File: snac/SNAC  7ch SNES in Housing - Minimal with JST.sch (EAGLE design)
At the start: 8 parts, among them U1 PMIC-LDO-XC6206P332MR-G(SOT23), X2 JST-XH-09-PIN-LONG-PAD

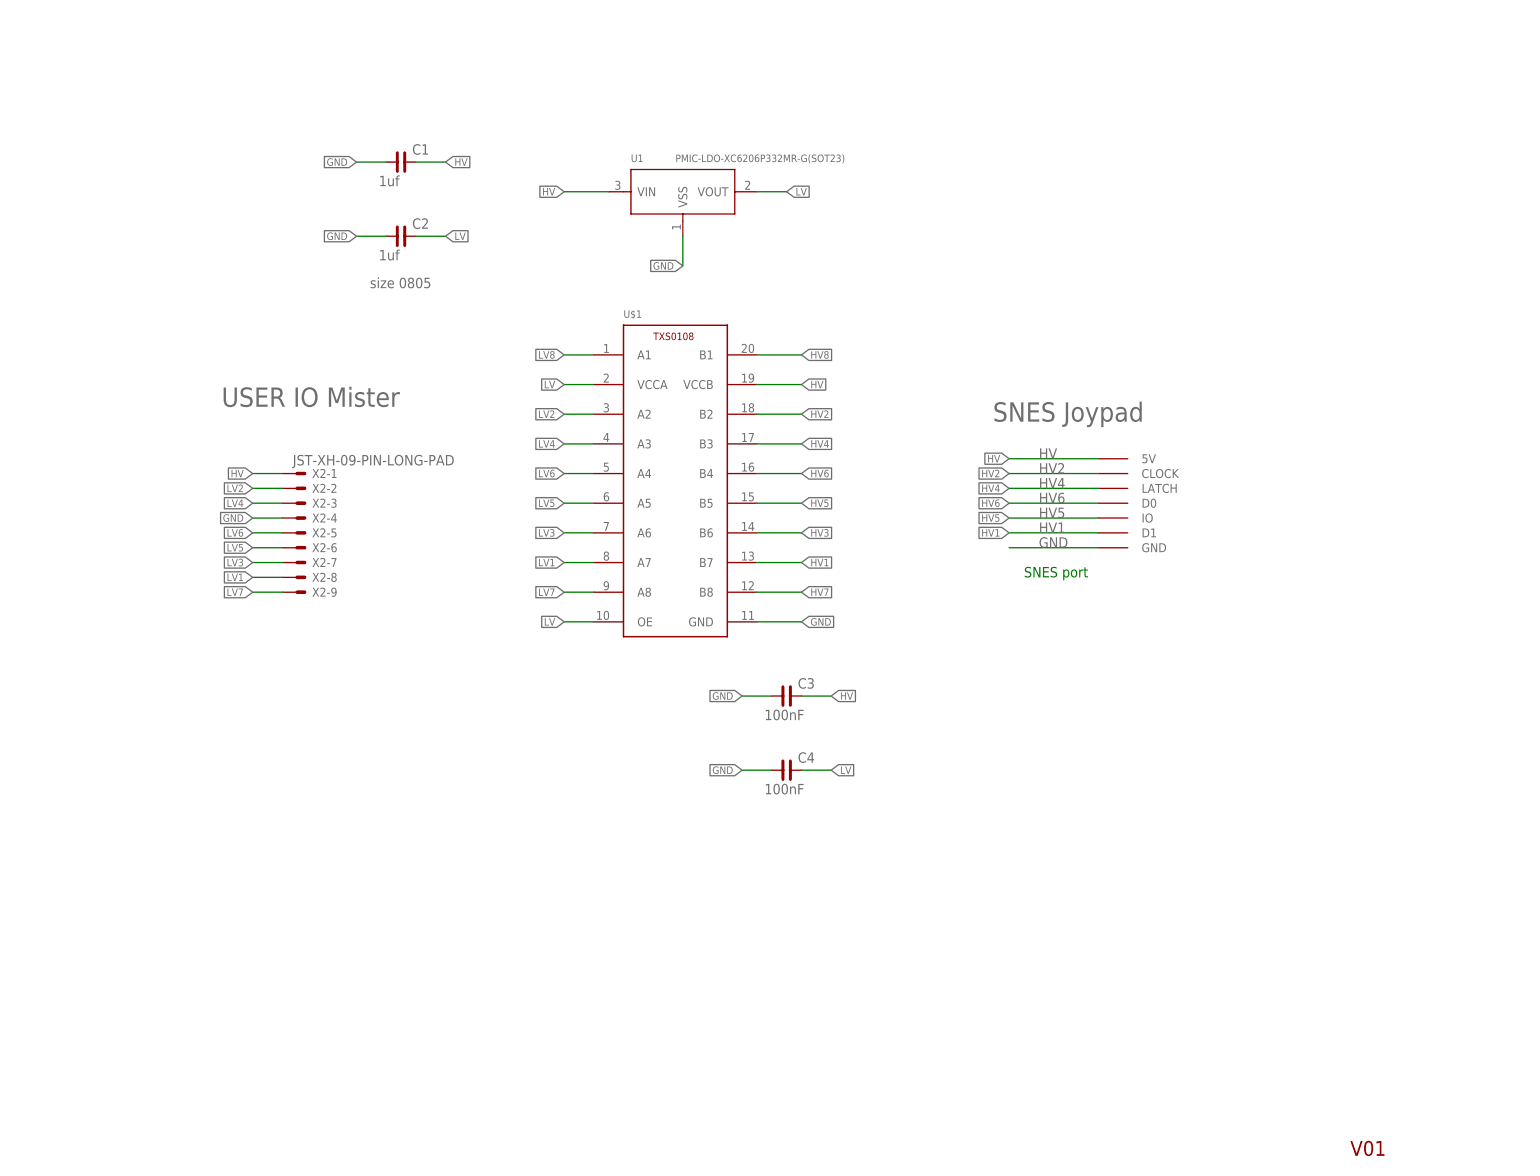
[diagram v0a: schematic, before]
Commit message: added reversed JST footprint to SNES SNAC Minimal
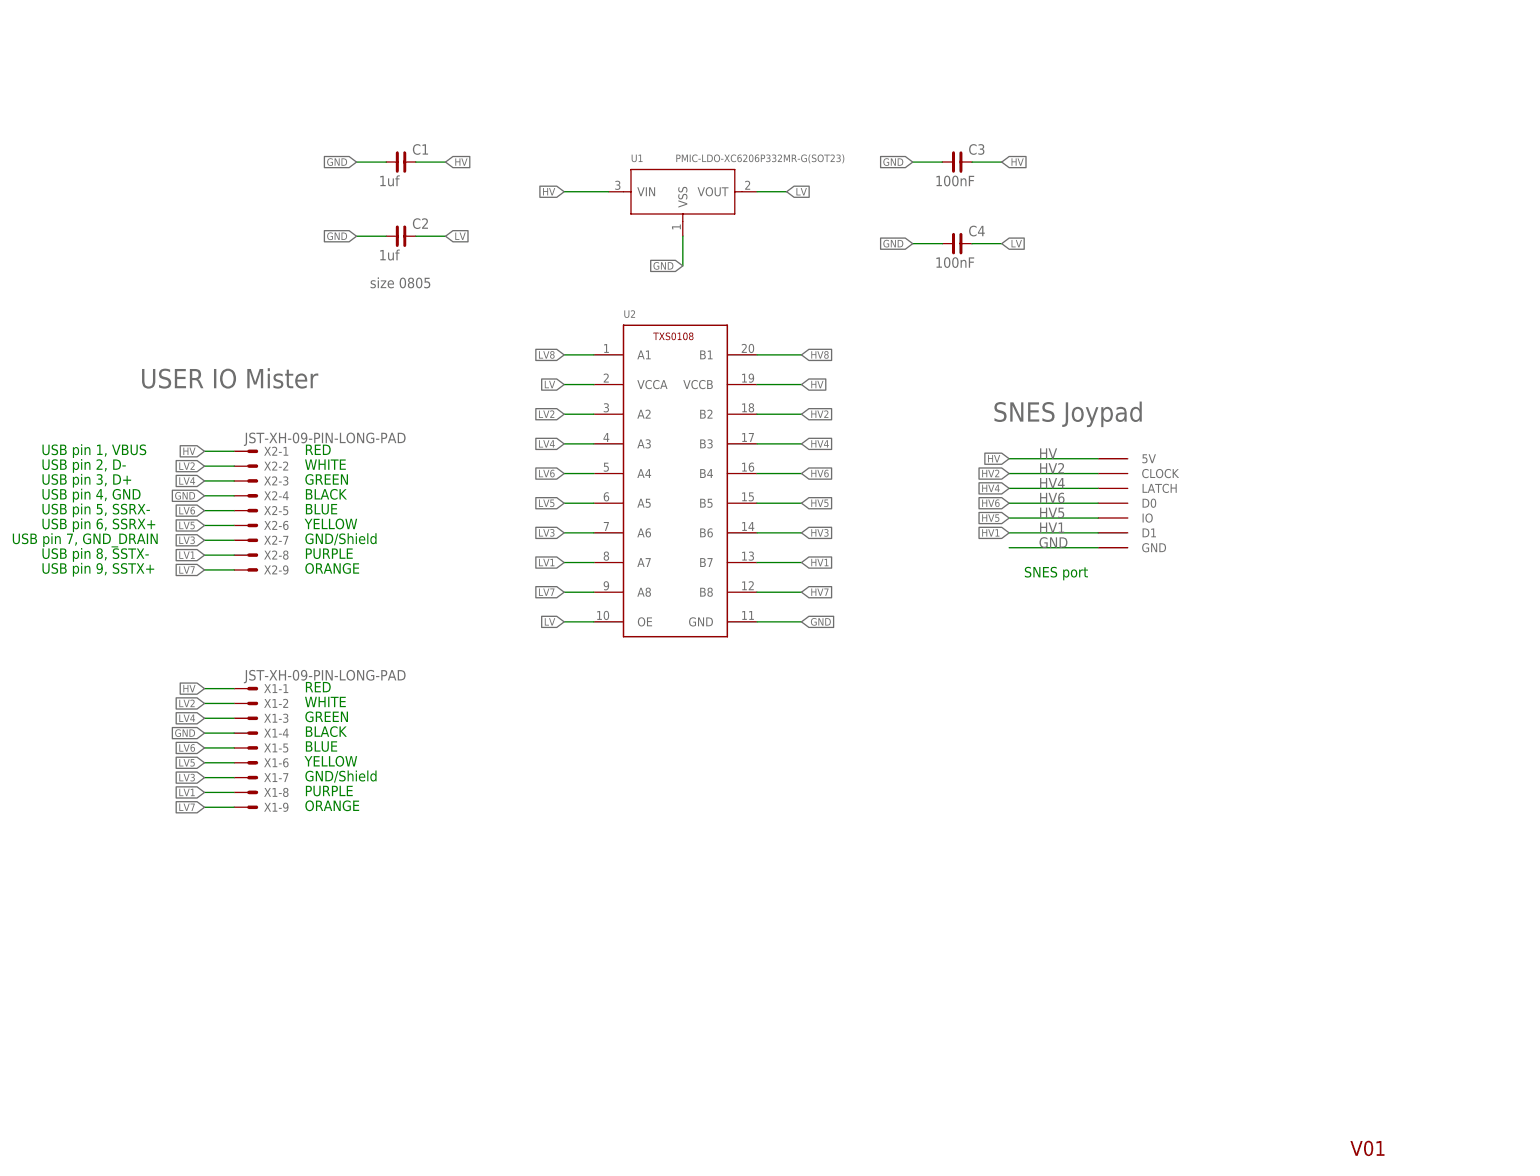
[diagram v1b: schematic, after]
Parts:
- added X1: JST-XH-09-PIN-LONG-PAD, Rembrandt Electronics - JST XH Connectors v1-0:JST-XH-09-PIN-LONG-PAD
- renumbered U$1 to U2, U$3 to SNES_CON
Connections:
- net GND: now also X1-4.S
- net HV: now also X1-1.S
- net LV1: now also X1-8.S
- net LV2: now also X1-2.S
- net LV3: now also X1-7.S
- net LV4: now also X1-3.S
- net LV5: now also X1-6.S
- net LV6: now also X1-5.S
- net LV7: now also X1-9.S
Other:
- note added: "BLACK"
- note added: "BLUE"
- note added: "GND/Shield"
- note added: "GREEN"
- note added: "ORANGE"
- note added: "PURPLE"
- note added: "RED"
- note added: "USB pin 1, VBUS"
- note added: "USB pin 2, D-"
- note added: "USB pin 3, D+"
- note added: "USB pin 4, GND"
- note added: "USB pin 5, SSRX-"
- note added: "USB pin 6, SSRX+"
- note added: "USB pin 7, GND_DRAIN"
- note added: "USB pin 8, SSTX-"
- note added: "USB pin 9, SSTX+"
- note added: "WHITE"
- note added: "YELLOW"
- moved on the sheet: C3, C4, X2-1, X2-2, X2-3, X2-4, X2-5, X2-6, X2-7, X2-8, X2-9

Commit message: removed the Compact, TXS chip, and SMS3D with USB3 plug versions
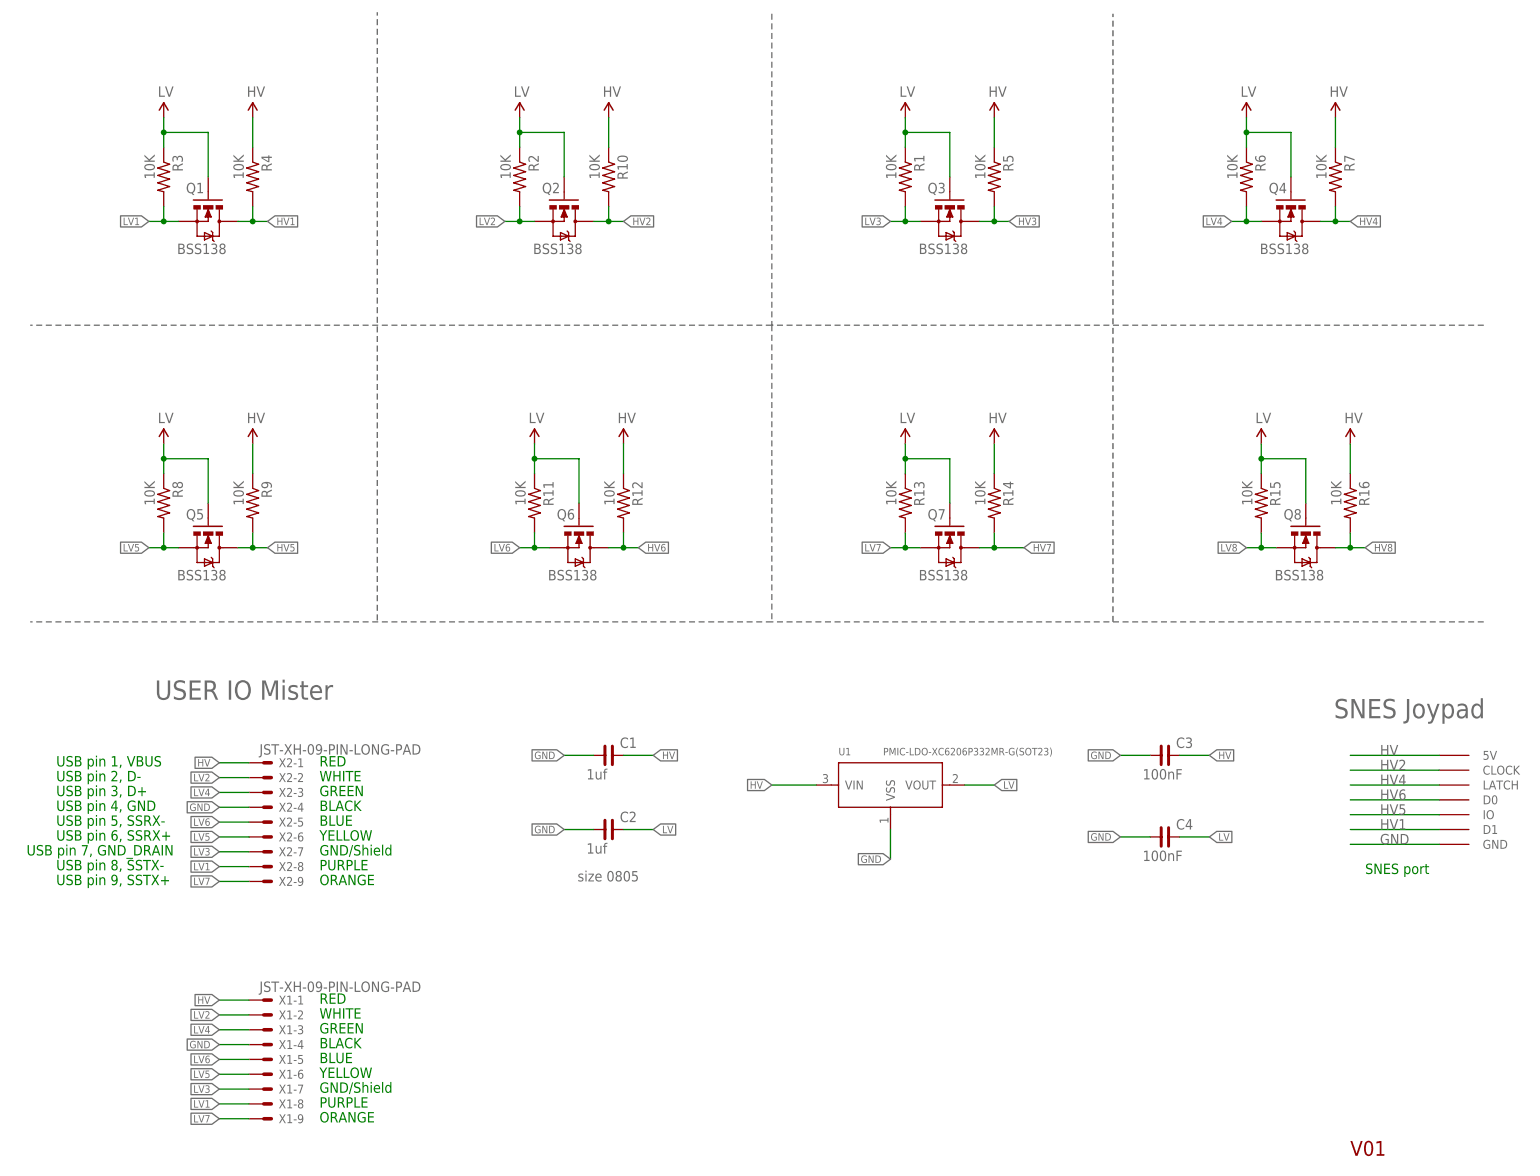
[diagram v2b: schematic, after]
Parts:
- removed U2: TXS0108, FaBo-LevelTranslator:TXS0108
- added Q1, Q2, Q3, Q4, Q5, Q6, Q7, Q8: BSS138, SparkFun:MOSFET-NCHANNELSMD
- added R1, R10, R11, R12, R13, R14, R15, R16, R2, R3, R4, R5, R6, R7, R8, R9: 10K, SparkFun:RESISTOR0603-RES
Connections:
- net GND: no longer U2.GND
- net HV: now also R10.1, R12.1, R14.1, R16.1, R4.1, R5.1, R7.1, R9.1; no longer U2.VCCB
- net HV1: now also Q1.D, R4.2; no longer U2.B7
- net HV2: now also Q2.D, R10.2; no longer U2.B2
- net HV3: now also Q3.D, R5.2; no longer U2.B6
- net HV4: now also Q4.D, R7.2; no longer U2.B3
- net HV5: now also Q5.D, R9.2; no longer U2.B5
- net HV6: now also Q6.D, R12.2; no longer U2.B4
- net HV7: now also Q7.D, R14.2; no longer U2.B8
- net HV8: now also Q8.D, R16.2; no longer U2.B1
- net LV: now also Q1.G, Q2.G, Q3.G, Q4.G, Q5.G, Q6.G, Q7.G, Q8.G, R1.1, R11.1, R13.1, R15.1, R2.1, R3.1, R6.1, R8.1; no longer U2.OE, U2.VCCA
- net LV1: now also Q1.S, R3.2; no longer U2.A7
- net LV2: now also Q2.S, R2.2; no longer U2.A2
- net LV3: now also Q3.S, R1.2; no longer U2.A6
- net LV4: now also Q4.S, R6.2; no longer U2.A3
- net LV5: now also Q5.S, R8.2; no longer U2.A5
- net LV6: now also Q6.S, R11.2; no longer U2.A4
- net LV7: now also Q7.S, R13.2; no longer U2.A8
- net LV8: now also Q8.S, R15.2; no longer U2.A1
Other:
- moved on the sheet: C1, C2, C3, C4, U1, X1-1, X1-2, X1-3, X1-4, X1-5, X1-6, X1-7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

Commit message: removed one cap from the SNES SNAC JST, as it was overkill
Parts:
- removed C4: 100nF, rc-master-smd:C_0805
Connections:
- net GND: no longer C4.1
- net HV: no longer C3.2
- net LV: now also C3.2; no longer C4.2
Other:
- moved on the sheet: C3
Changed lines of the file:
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@@
 <part name="X2" library="Rembrandt Electronics - JST XH Connectors v1-0" deviceset="JST-XH-09-PIN" device="-LONG-PAD"/>
 <part name="C3" library="rc-master-smd" deviceset="C_" device="0805" value="100nF"/>
-<part name="C4" library="rc-master-smd" deviceset="C_" device="0805" value="100nF"/>
 <part name="X1" library="Rembrandt Electronics - JST XH Connectors v1-0" deviceset="JST-XH-09-PIN" device="-LONG-PAD"/>
 <part name="Q4" library="SparkFun" deviceset="MOSFET-NCHANNEL" device="SMD" value="BSS138"/>
@@
 <instance part="X2" gate="-8" x="55.245" y="97.79"/>
 <instance part="X2" gate="-9" x="55.245" y="95.25"/>
-<instance part="C3" gate="G$1" x="209.55" y="116.84"/>
-<instance part="C4" gate="G$1" x="209.55" y="102.87"/>
+<instance part="C3" gate="G$1" x="209.55" y="102.87"/>
 <instance part="X1" gate="-1" x="55.245" y="74.93"/>
 <instance part="X1" gate="-2" x="55.245" y="72.39"/>
@@
 </segment>
 <segment>
-<pinref part="C4" gate="G$1" pin="2"/>
+<pinref part="C3" gate="G$1" pin="2"/>
 <wire x1="212.09" y1="102.87" x2="217.17" y2="102.87" width="0.1524" layer="91"/>
 <label x="217.17" y="102.87" size="1.27" layer="95" xref="yes"/>
@@
 </segment>
 <segment>
-<pinref part="C3" gate="G$1" pin="2"/>
-<wire x1="212.09" y1="116.84" x2="217.17" y2="116.84" width="0.1524" layer="91"/>
-<label x="217.17" y="116.84" size="1.27" layer="95" xref="yes"/>
-</segment>
-<segment>
 <wire x1="52.705" y1="74.93" x2="47.625" y2="74.93" width="0.1524" layer="91"/>
 <label x="47.625" y="74.93" size="1.27" layer="95" rot="MR0" xref="yes"/>
@@
 <segment>
 <pinref part="C3" gate="G$1" pin="1"/>
-<wire x1="207.01" y1="116.84" x2="201.93" y2="116.84" width="0.1524" layer="91"/>
-<label x="201.93" y="116.84" size="1.27" layer="95" rot="MR0" xref="yes"/>
-</segment>
-<segment>
-<pinref part="C4" gate="G$1" pin="1"/>
 <wire x1="207.01" y1="102.87" x2="201.93" y2="102.87" width="0.1524" layer="91"/>
 <label x="201.93" y="102.87" size="1.27" layer="95" rot="MR0" xref="yes"/>
